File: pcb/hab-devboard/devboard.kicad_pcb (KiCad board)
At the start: 4 copper layers, 86.3 x 120 mm, 86 parts, among them J1 S2B-PH-K-S, J2 SM04B-GHS-TB, J3 SM04B-GHS-TB, J4 2x20 Pin Header, J5 S2B-PH-K-S, Q1 DMG2301L, Q2 CSD25310Q2, Q3 BSS138, Q4 BSS138, Q5 BSS138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

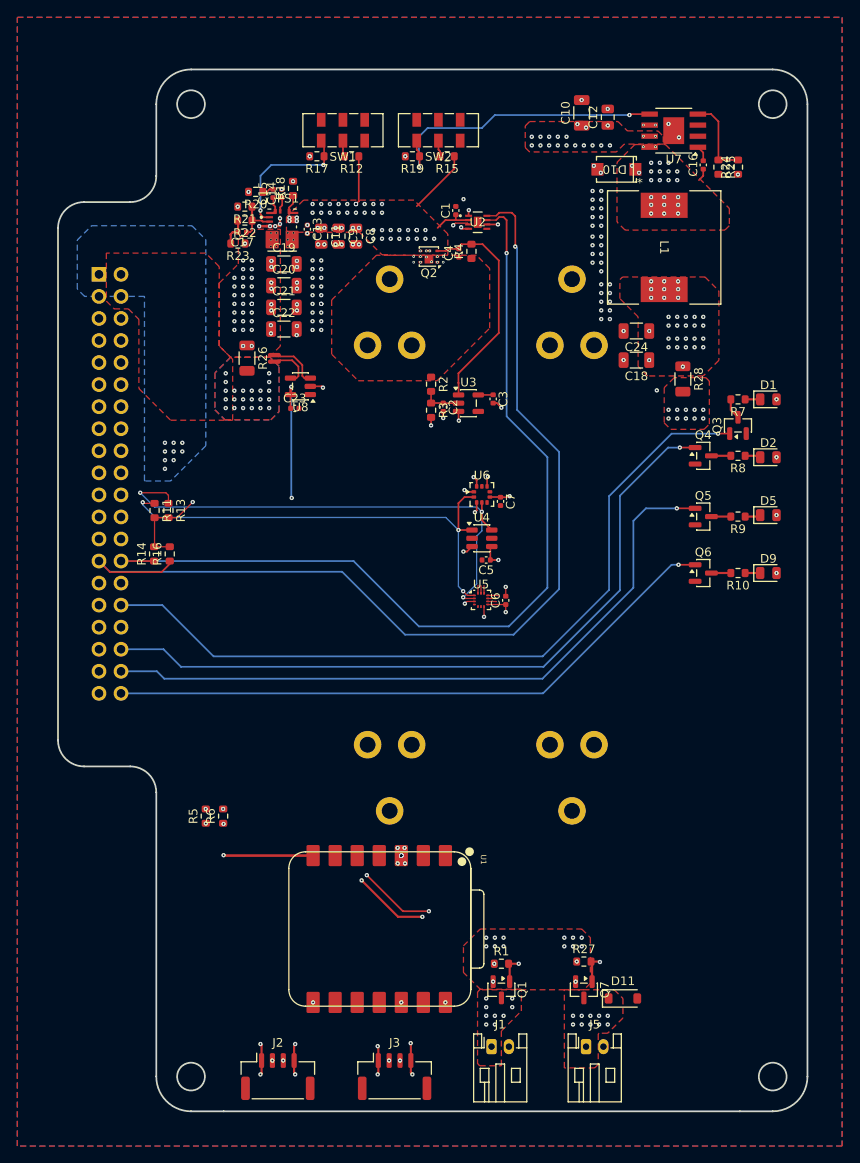
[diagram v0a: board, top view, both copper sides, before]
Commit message: Updating pcb, adding xcode project for macOS gui
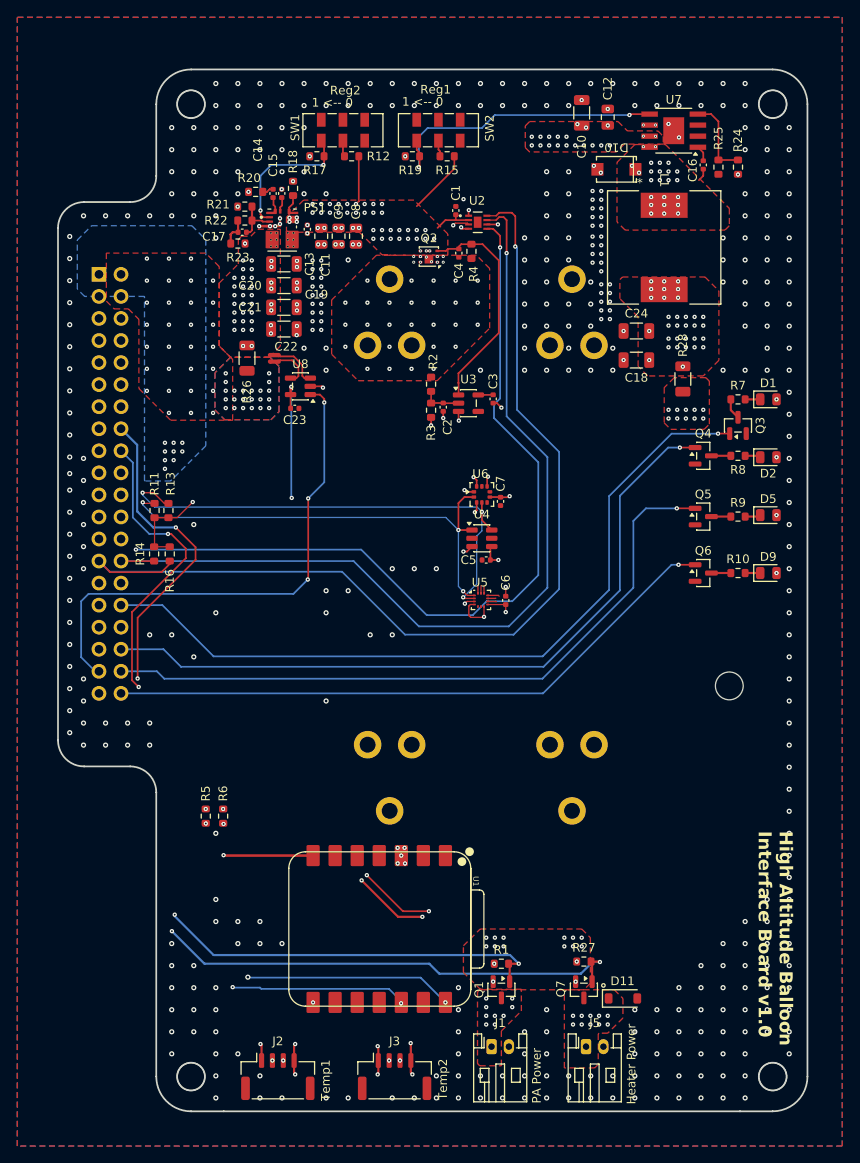
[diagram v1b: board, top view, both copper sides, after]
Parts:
- added H1: MountingHole, MountingHole:MountingHole_3.2mm_M3, F.Cu at (123.6, 39.2)
- added H2: MountingHole, MountingHole:MountingHole_3.2mm_M3, F.Cu at (190.6, 39.2)
- added H3: MountingHole, MountingHole:MountingHole_3.2mm_M3, F.Cu at (190.6, 151.2)
- added H4: MountingHole, MountingHole:MountingHole_3.2mm_M3, F.Cu at (123.6, 151.2)
- added H5: MountingHole, MountingHole:MountingHole_3.2mm_M3, F.Cu at (185.6, 106.2)
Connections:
- J4 pad 16: unconnected-(J4-Pin_16-Pad16) -> /5V_PA_EN
- J4 pad 18: unconnected-(J4-Pin_18-Pad18) -> /5V_HEATER_EN
- J4 pad 31: unconnected-(J4-Pin_31-Pad31) -> /BATT_ALERT_N
- J4 pad 33: unconnected-(J4-Pin_33-Pad33) -> /GPS_WAKE
- J4 pad 35: unconnected-(J4-Pin_35-Pad35) -> /GPS_RST_N
- J4 pad 37: unconnected-(J4-Pin_37-Pad37) -> /5V_SNS
- U5 pad 4: unconnected-(U5-~{CS}-Pad4) -> +3V3_SBC
- U8 pad 1: /5VSNS -> /5V_SNS
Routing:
- net /5V_HEATER_EN: track 3.41 -> 119.8 mm, vias 1 -> 4
- net /5V_PA_EN: track 3.29 -> 110.9 mm, vias 1 -> 4
- net /BATT_ALERT_N: track 0.00 -> 104.3 mm, vias 0 -> 2
- net /GPS_WAKE: track 0.00 -> 73.0 mm, vias 1 -> 2
- net /GPS_RST_N: track 0.00 -> 67.3 mm, vias 1 -> 2
- net /5V_SNS: track 0.00 -> 59.7 mm, vias 0 -> 3
- net +3V3_SBC: track 107.7 -> 109.3 mm, vias 39 -> 27
- net /I2C_SNS_SDA: track 182.3 -> 181.5 mm
- net /UART2_RX_M0: track 60.2 -> 60.7 mm
- net GND: vias 102 -> 447
- net /5V_SUPPLY_2: vias 37 -> 36
- net +VBAT: vias 10 -> 37
- net +PACK: vias 69 -> 67
- net +5V: vias 53 -> 82
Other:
- board text added: "1 <-- 0"
- board text added: "Heater Power"
- board text added: "High Altitude Balloon Interface Board v1.0"
- board text added: "PA Power"
- board text added: "Reg1"
- board text added: "Reg2"
- board text added: "Temp1"
- board text added: "Temp2"
